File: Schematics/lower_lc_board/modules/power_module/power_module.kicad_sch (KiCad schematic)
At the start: 33 parts, among them J1 Stack Male Edge Connector, U1 TVS3300DRV, U10 ID_LM66100DCKR, U2 AMS1117, U3 ID_LM66100DCKR, U4 ID_LM66100DCKR

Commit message: more local pours and 0402 adjustments
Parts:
- C51, C52: footprint Capacitor_SMD:C_0402_1005Metric -> Capacitor_SMD:C_0603_1608Metric
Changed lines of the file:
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@@
 			)
 		)
-		(property "Footprint" "Capacitor_SMD:C_0402_1005Metric"
+		(property "Footprint" "Capacitor_SMD:C_0603_1608Metric"
 			(at 208.28 61.2648 0)
 			(effects
@@
 			)
 		)
-		(property "Footprint" "Capacitor_SMD:C_0402_1005Metric"
+		(property "Footprint" "Capacitor_SMD:C_0603_1608Metric"
 			(at 208.28 49.8348 0)
 			(effects

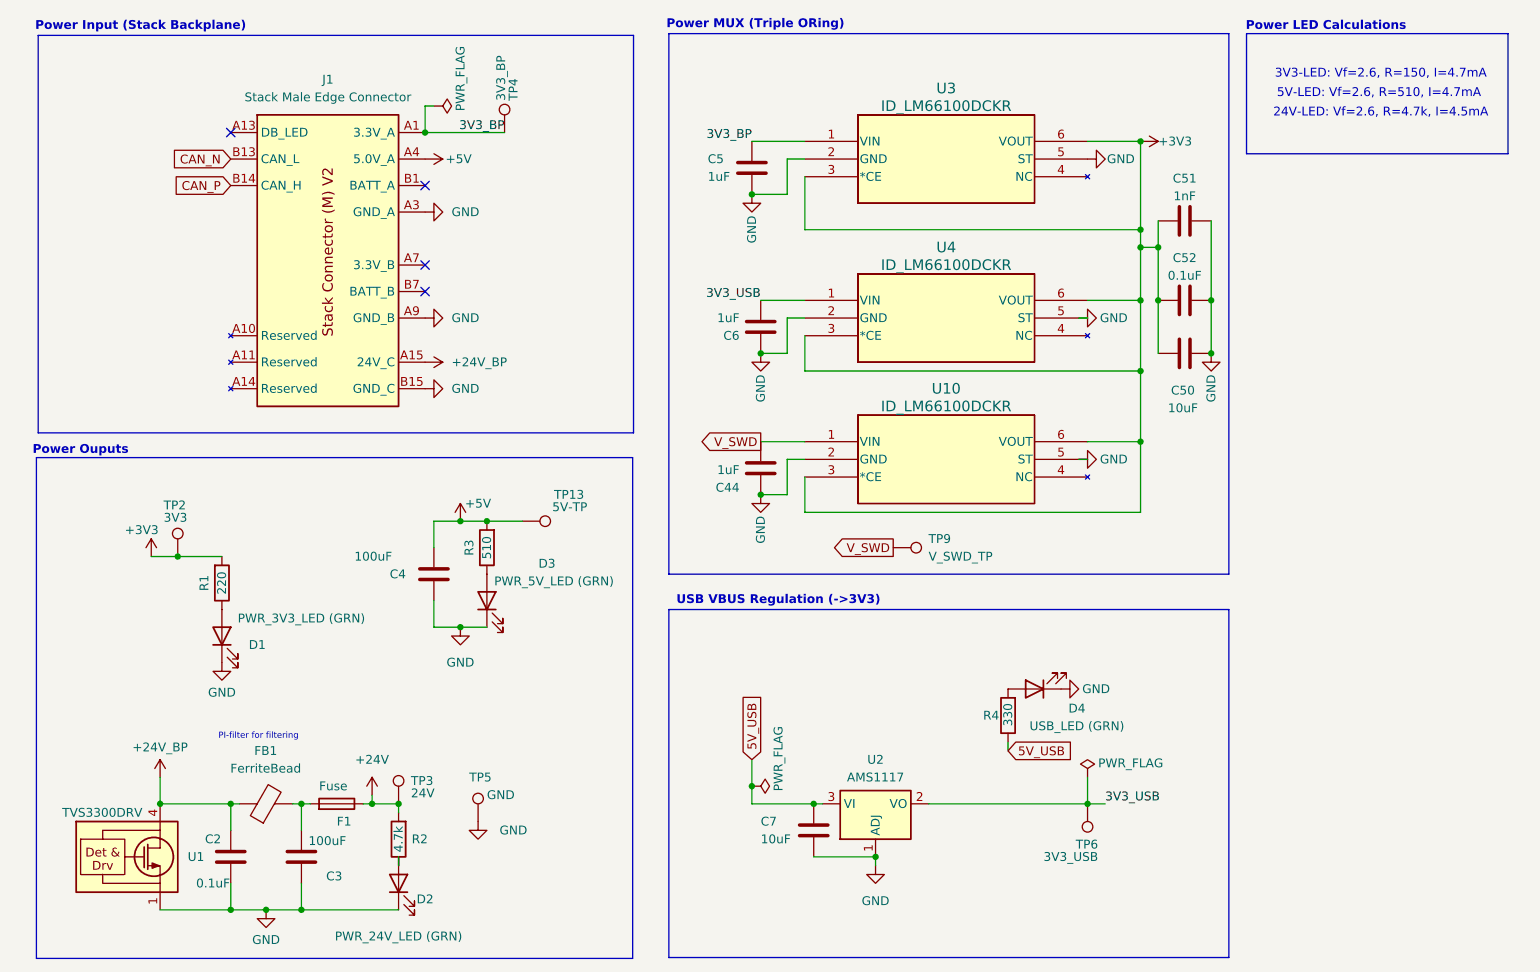
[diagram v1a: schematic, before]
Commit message: review of schematics and pcb
- verified all STM pins
- reviewed all circuits
- reviewed trace clearences, made sure routes are connected, etc.
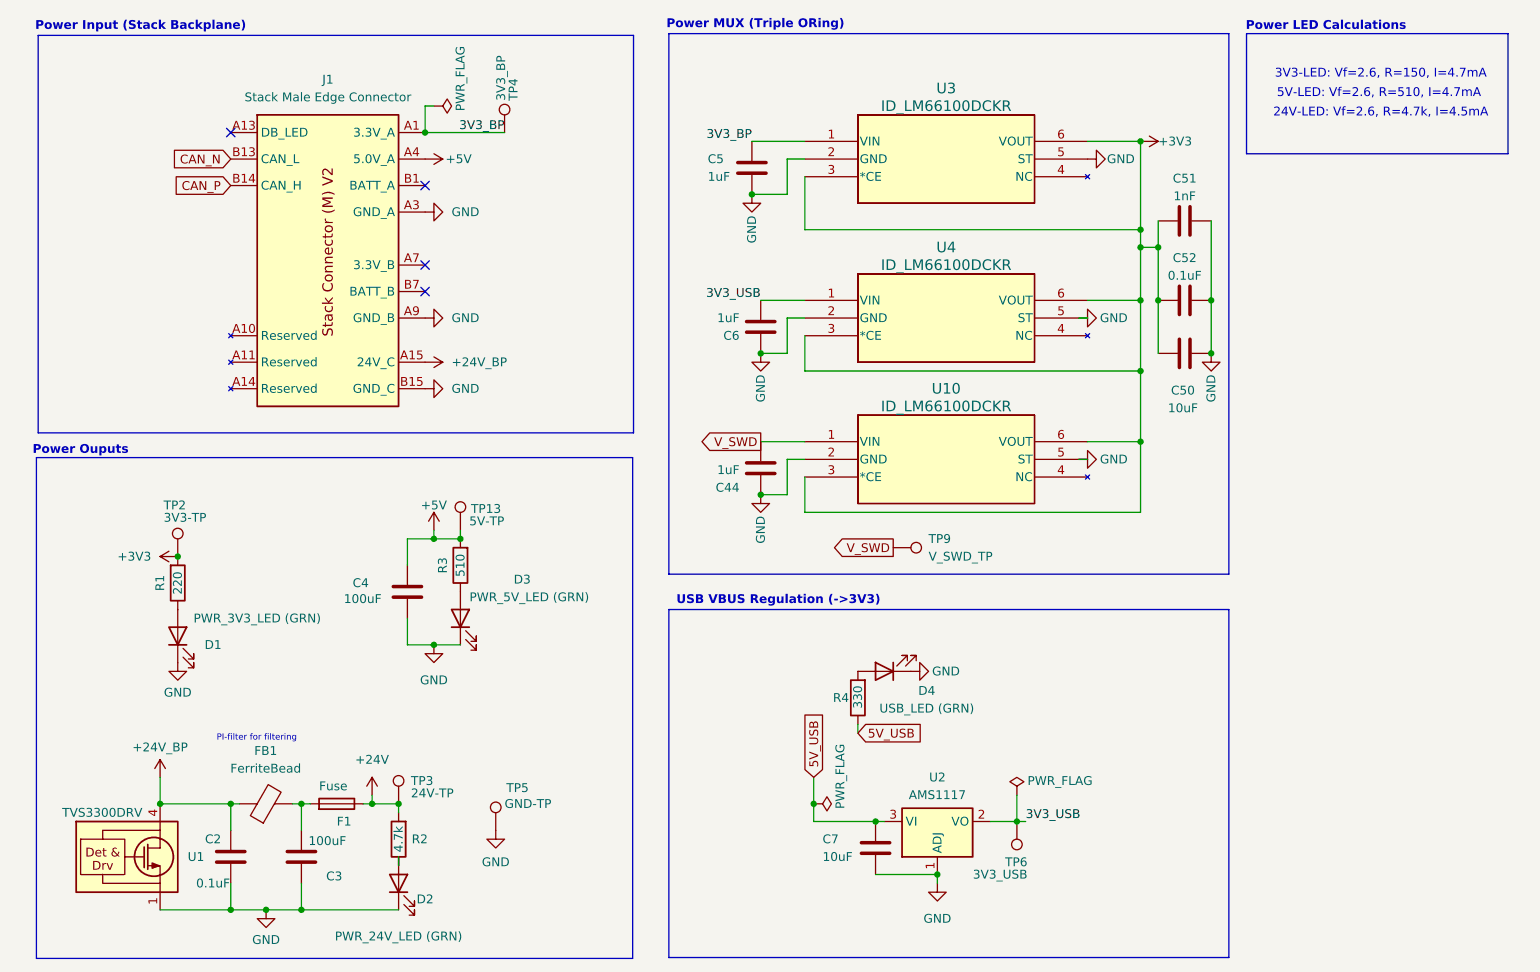
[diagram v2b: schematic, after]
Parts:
- C51: JLCPCB C1523 -> C1588
- C52: JLCPCB C1525 -> C14663
- R2: JLCPCB (none) -> C17936
- TP2: value 3V3 -> 3V3-TP
- TP3: value 24V -> 24V-TP
- TP5: value GND -> GND-TP
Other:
- moved on the sheet: C4, C7, D1, D3, D4, R1, R3, R4, TP13, TP5, TP6, U2

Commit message: silkscreen
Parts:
- removed TP3: 24V-TP, TestPoint:TestPoint_Pad_D1.0mm, symbol Connector:TestPoint
- added TP1: 24V-TP, TestPoint:TestPoint_Pad_D1.0mm, symbol Connector:TestPoint
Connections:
- net +24V: now also TP1.1
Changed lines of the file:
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@@
 	)
 	(junction
-		(at 91.44 134.62)
-		(diameter 0)
-		(color 0 0 0 0)
-	)
-	(junction
 		(at 208.28 69.85)
 		(diameter 0)
@@
 	)
 	(junction
+		(at 91.44 134.62)
+		(diameter 0)
+		(color 0 0 0 0)
+	)
+	(junction
 		(at 67.31 149.86)
 		(diameter 0)
@@
 	)
 	(symbol
-		(lib_id "Connector:TestPoint")
-		(at 91.44 134.62 0)
-		(unit 1)
-		(exclude_from_sim no)
-		(in_bom yes)
-		(on_board yes)
-		(dnp no)
-		(property "Reference" "TP3"
-			(at 93.218 131.318 0)
-			(effects
-				(font
-					(size 1.27 1.27)
-				)
-				(justify left)
-			)
-		)
-		(property "Value" "24V-TP"
-			(at 93.218 133.096 0)
-			(effects
-				(font
-					(size 1.27 1.27)
-				)
-				(justify left)
-			)
-		)
-		(property "Footprint" "TestPoint:TestPoint_Pad_D1.0mm"
-			(at 96.52 134.62 0)
-			(effects
-				(font
-					(size 1.27 1.27)
-				)
-				(hide yes)
-			)
-		)
-		(property "Datasheet" "~"
-			(at 96.52 134.62 0)
-			(effects
-				(font
-					(size 1.27 1.27)
-				)
-				(hide yes)
-			)
-		)
-		(property "Description" "test point"
-			(at 91.44 134.62 0)
-			(effects
-				(font
-					(size 1.27 1.27)
-				)
-				(hide yes)
-			)
-		)
-		(pin "1"
-		)
-		(instances
-			(project "lower_lc_board"
-				(path "/d63798c4-e363-437e-9012-e4aff32e6642/ea1dc739-d1f4-46a0-a090-2a1bf39da427"
-					(reference "TP3")
-					(unit 1)
-				)
-			)
-		)
-	)
-	(symbol
 		(lib_id "power:PWR_FLAG")
 		(at 96.52 34.29 270)
@@
 					(unit 1)
 				)
+			)
+		)
+	)
+	(symbol
+		(lib_id "Connector:TestPoint")
+		(at 91.44 134.62 0)
+		(unit 1)
+		(exclude_from_sim no)
+		(in_bom yes)
+		(on_board yes)
+		(dnp no)
+		(property "Reference" "TP1"
+			(at 93.218 131.318 0)
+			(effects
+				(font
+					(size 1.27 1.27)
+				)
+				(justify left)
+			)
+		)
+		(property "Value" "24V-TP"
+			(at 93.218 133.096 0)
+			(effects
+				(font
+					(size 1.27 1.27)
+				)
+				(justify left)
+			)
+		)
+		(property "Footprint" "TestPoint:TestPoint_Pad_D1.0mm"
+			(at 96.52 134.62 0)
+			(effects
+				(font
+					(size 1.27 1.27)
+				)
+				(hide yes)
+			)
+		)
+		(property "Datasheet" "~"
+			(at 96.52 134.62 0)
+			(effects
+				(font
+					(size 1.27 1.27)
+				)
+				(hide yes)
+			)
+		)
+		(property "Description" "test point"
+			(at 91.44 134.62 0)
+			(effects
+				(font
+					(size 1.27 1.27)
+				)
+				(hide yes)
+			)
+		)
+		(pin "1"
+		)
+		(instances
+			(project "lower_lc_board"
+				(path "/d63798c4-e363-437e-9012-e4aff32e6642/ea1dc739-d1f4-46a0-a090-2a1bf39da427"
+					(reference "TP1")
+					(unit 1)
+				)

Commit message: remove surge protector
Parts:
- removed U1: TVS3300DRV, Package_SON:WSON-6-1EP_2x2mm_P0.65mm_EP1x1.6mm, symbol Power_Protection:TVS3300DRV
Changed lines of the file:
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@@
 	)
 	(junction
-		(at 67.31 149.86)
-		(diameter 0)
-		(color 0 0 0 0)
-	)
-	(junction
 		(at 198.12 82.55)
 		(diameter 0)
@@
 	)
 	(junction
-		(at 57.15 134.62)
-		(diameter 0)
-		(color 0 0 0 0)
-	)
-	(junction
 		(at 59.69 99.06)
 		(diameter 0)
@@
 	(wire
 		(pts
-			(xy 57.15 149.86) (xy 67.31 149.86)
-		)
-		(stroke
-			(width 0)
-			(type default)
-		)
-	)
-	(wire
-		(pts
 			(xy 92.71 96.52) (xy 96.52 96.52)
 		)
@@
 	(wire
 		(pts
-			(xy 57.15 134.62) (xy 57.15 130.81)
-		)
-		(stroke
-			(width 0)
-			(type default)
-		)
-	)
-	(wire
-		(pts
 			(xy 198.12 72.39) (xy 198.12 82.55)
 		)
@@
 	(wire
 		(pts
-			(xy 57.15 134.62) (xy 67.31 134.62)
-		)
-		(stroke
-			(width 0)
-			(type default)
-		)
-	)
-	(wire
-		(pts
 			(xy 95.25 34.29) (xy 96.52 34.29)
 		)
@@
 	)
 	(symbol
-		(lib_id "Power_Protection:TVS3300DRV")
-		(at 57.15 142.24 0)
-		(unit 1)
-		(exclude_from_sim no)
-		(in_bom yes)
-		(on_board yes)
-		(dnp no)
-		(property "Reference" "U1"
-			(at 63.5 142.24 0)
-			(effects
-				(font
-					(size 1.27 1.27)
-				)
-				(justify right)
-			)
-		)
-		(property "Value" "TVS3300DRV"
-			(at 54.61 135.89 0)
-			(effects
-				(font
-					(size 1.27 1.27)
-				)
-				(justify right)
-			)
-		)
-		(property "Footprint" "Package_SON:WSON-6-1EP_2x2mm_P0.65mm_EP1x1.6mm"
-			(at 62.23 151.13 0)
-			(effects
-				(font
-					(size 1.27 1.27)
-				)
-				(hide yes)
-			)
-		)
-		(property "Datasheet" "${KIPRJMOD}/../../Documentation/surgeprot_tvs3300_DS.pdf"
-			(at 54.61 142.24 0)
-			(effects
-				(font
-					(size 1.27 1.27)
-				)
-				(hide yes)
-			)
-		)
-		(property "Description" "Flat-Clamp Surge Protection Device. 33Vrwm, WSON-6"
-			(at 57.15 142.24 0)
-			(effects
-				(font
-					(size 1.27 1.27)
-				)
-				(hide yes)
-			)
-		)
-		(property "LCSC" "C2863624"
-			(at 57.15 142.24 0)
-			(effects
-				(font
-					(size 1.27 1.27)
-				)
-				(hide yes)
-			)
-		)
-		(pin "7"
-		)
-		(pin "6"
-		)
-		(pin "4"
-		)
-		(pin "5"
-		)
-		(pin "1"
-		)
-		(pin "3"
-		)
-		(pin "2"
-		)
-		(instances
-			(project "lower_lc_board"
-				(path "/d63798c4-e363-437e-9012-e4aff32e6642/ea1dc739-d1f4-46a0-a090-2a1bf39da427"
-					(reference "U1")
-					(unit 1)
-				)
-			)
-		)
-	)
-	(symbol
 		(lib_id "Connector:TestPoint")
 		(at 180.34 137.16 180)
@@
 	(symbol
 		(lib_id "power:+24V")
-		(at 57.15 130.81 0)
+		(at 67.31 134.62 90)
 		(unit 1)
 		(exclude_from_sim no)
@@
 		(dnp no)
 		(property "Reference" "#PWR02"
-			(at 57.15 134.62 0)
+			(at 71.12 134.62 0)
 			(effects
 				(font
@@
 		)
 		(property "Value" "+24V_BP"
-			(at 57.15 126.492 0)
+			(at 59.182 134.62 90)
 			(effects
 				(font
@@
 		)
 		(property "Footprint" ""
-			(at 57.15 130.81 0)
+			(at 67.31 134.62 0)
 			(effects
 				(font
@@
 		)
 		(property "Datasheet" ""
-			(at 57.15 130.81 0)
+			(at 67.31 134.62 0)
 			(effects
 				(font
@@
 		)
 		(property "Description" "Power symbol creates a global label with name \"+24V\""
-			(at 57.15 130.81 0)
+			(at 67.31 134.62 0)
 			(effects
 				(font

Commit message: put TH on backside, add edge-vias
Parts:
- added TP3: GND-TP-H, TestPoint:TestPoint_THTPad_D1.0mm_Drill0.5mm, symbol Connector:TestPoint
- TP5: value GND-TP -> GND-TP-P; footprint TestPoint:TestPoint_Pad_D1.0mm -> TestPoint:TestPoint_Pad_1.5x1.5mm
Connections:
- net GND: now also TP3.1
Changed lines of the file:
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@@
 			)
 		)
-		(property "Value" "GND-TP"
+		(property "Value" "GND-TP-P"
 			(at 106.68 134.62 0)
 			(effects
@@
 			)
 		)
-		(property "Footprint" "TestPoint:TestPoint_Pad_D1.0mm"
+		(property "Footprint" "TestPoint:TestPoint_Pad_1.5x1.5mm"
 			(at 110.49 138.43 0)
 			(effects
@@
 	)
 	(symbol
+		(lib_id "Connector:TestPoint")
+		(at 111.76 143.51 0)
+		(unit 1)
+		(exclude_from_sim no)
+		(in_bom yes)
+		(on_board yes)
+		(dnp no)
+		(property "Reference" "TP3"
+			(at 113.284 137.414 0)
+			(effects
+				(font
+					(size 1.27 1.27)
+				)
+				(justify left)
+			)
+		)
+		(property "Value" "GND-TP-H"
+			(at 113.03 139.7 0)
+			(effects
+				(font
+					(size 1.27 1.27)
+				)
+				(justify left)
+			)
+		)
+		(property "Footprint" "TestPoint:TestPoint_THTPad_D1.0mm_Drill0.5mm"
+			(at 116.84 143.51 0)
+			(effects
+				(font
+					(size 1.27 1.27)
+				)
+				(hide yes)
+			)
+		)
+		(property "Datasheet" "~"
+			(at 116.84 143.51 0)
+			(effects
+				(font
+					(size 1.27 1.27)
+				)
+				(hide yes)
+			)
+		)
+		(property "Description" "test point"
+			(at 111.76 143.51 0)
+			(effects
+				(font
+					(size 1.27 1.27)
+				)
+				(hide yes)
+			)
+		)
+		(pin "1"
+		)
+		(instances
+			(project "lower_lc_board"
+				(path "/d63798c4-e363-437e-9012-e4aff32e6642/ea1dc739-d1f4-46a0-a090-2a1bf39da427"
+					(reference "TP3")
+					(unit 1)
+				)
+			)
+		)
+	)
+	(symbol
 		(lib_id "QRET_Buck_PSU:LM66100DCKR")
 		(at 170.18 64.77 0)
@@
 					(unit 1)
 				)
+			)
+		)
+	)
+	(symbol
+		(lib_id "power:GND")
+		(at 111.76 143.51 0)
+		(unit 1)
+		(exclude_from_sim no)
+		(in_bom yes)
+		(on_board yes)
+		(dnp no)
+		(property "Reference" "#PWR0109"
+			(at 111.76 149.86 0)
+			(effects
+				(font
+					(size 1.27 1.27)
+				)
+				(hide yes)
+			)
+		)
+		(property "Value" "GND"
+			(at 111.76 148.082 0)
+			(effects
+				(font
+					(size 1.27 1.27)
+				)
+			)
+		)
+		(property "Footprint" ""
+			(at 111.76 143.51 0)
+			(effects
+				(font
+					(size 1.27 1.27)
+				)
+				(hide yes)
+			)
+		)
+		(property "Datasheet" ""
+			(at 111.76 143.51 0)
+			(effects
+				(font
+					(size 1.27 1.27)
+				)
+				(hide yes)
+			)
+		)
+		(property "Description" "Power symbol creates a global label with name \"GND\" , ground"
+			(at 111.76 143.51 0)
+			(effects
+				(font
+					(size 1.27 1.27)
+				)
+				(hide yes)
+			)
+		)
+		(pin "1"
+		)
+		(instances
+			(project "lower_lc_board"
+				(path "/d63798c4-e363-437e-9012-e4aff32e6642/ea1dc739-d1f4-46a0-a090-2a1bf39da427"
+					(reference "#PWR0109")
+					(unit 1)
+				)

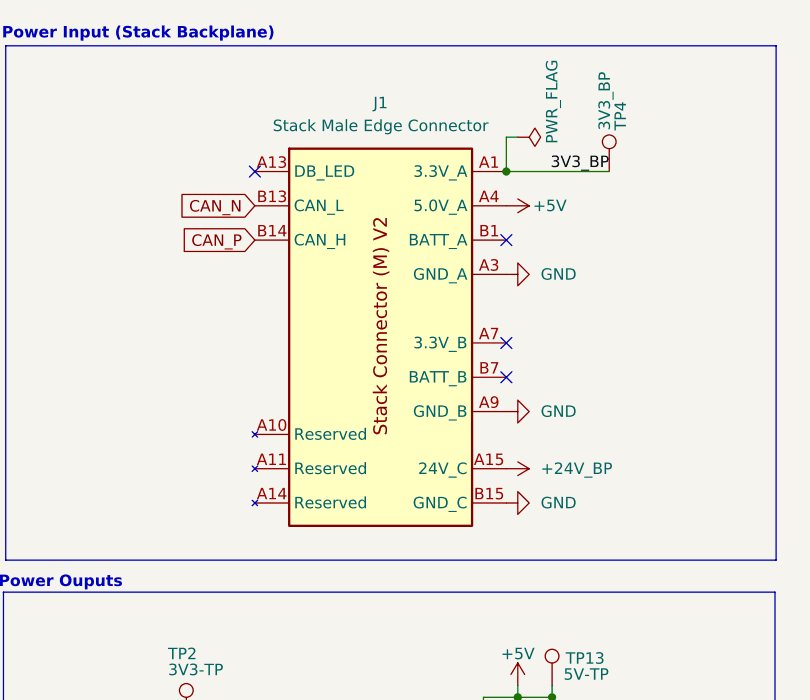
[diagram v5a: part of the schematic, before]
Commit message: new backplane connector
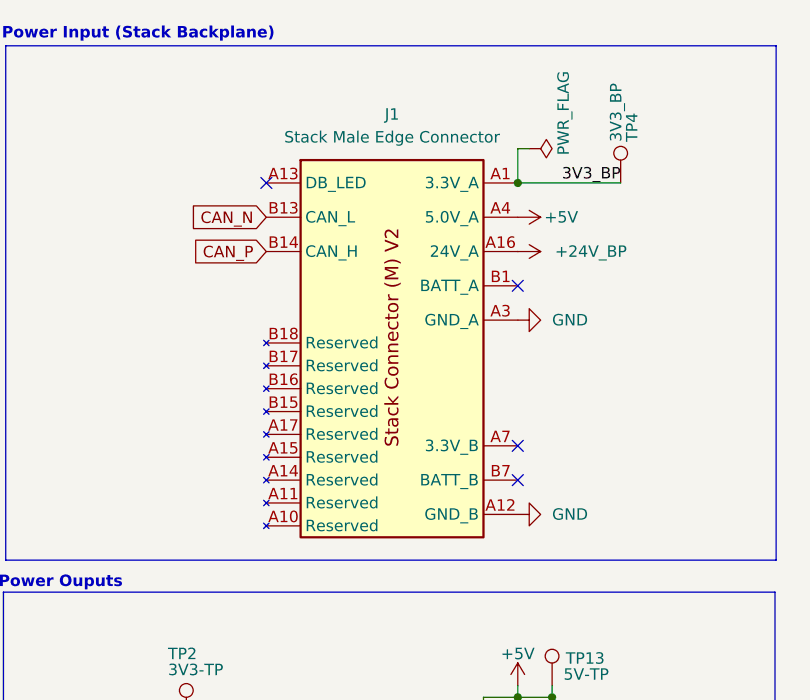
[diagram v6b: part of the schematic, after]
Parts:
- removed J1: Stack Male Edge Connector, Connector_PCBEdge:BUS_PCIexpress_x1, symbol EdgeConnector:Stack Male Edge Connector
- added J1: Stack Male Edge Connector, Connector_PCBEdge:BUS_PCIexpress_x1, symbol EdgeConnectorV2:Stack Male Edge Connector
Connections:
- net +24V_BP: now also J1.A16 (24V_A), J1.A18 (24V_A)
- net +5V: now also J1.A4 (5.0V_A), J1.A5 (5.0V_A)
- net 3V3_BP: now also J1.A1 (3.3V_A), J1.A2 (3.3V_A)
- net CAN_N: now also J1.B13 (CAN_L)
- net CAN_P: now also J1.B14 (CAN_H)
- net GND: now also J1.A12 (GND_B), J1.A3 (GND_A), J1.A6 (GND_A), J1.A9 (GND_B), J1.B10 (GND_B), J1.B11 (GND_B), J1.B12 (GND_B), J1.B4 (GND_A), J1.B5 (GND_A), J1.B6 (GND_A)
- new net: J1.A7 (3.3V_B), J1.A8 (3.3V_B)
- new net: J1.B1 (BATT_A), J1.B2 (BATT_A), J1.B3 (BATT_A)
- new net: J1.B7 (BATT_B), J1.B8 (BATT_B), J1.B9 (BATT_B)

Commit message: increase width on power rails from USB and SWD, start tuning diff pairs
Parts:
- C4: Digikey 732-8419-1-ND -> 732-8511-1-ND
- D1, D2, D3, D4: Digikey (none) -> 150080VS75000
- R1: JLCPCB (none) -> C22962
- R2: Digikey 311-4.70KFRCT-ND -> (none)
- R3: JLCPCB (none) -> C23186
- R4: JLCPCB (none) -> C23138
- U10, U3, U4: JLCPCB (none) -> C2869734
- U2: Digikey (none) -> 5399-AMS1117-3.3SOT-223TR-ND
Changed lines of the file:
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@@
 			)
 		)
+		(property "JLCPCB" "C2869734"
+			(at 170.18 41.91 0)
+			(effects
+				(font
+					(size 1.27 1.27)
+				)
+				(hide yes)
+			)
+		)
 		(pin "1"
 		)
@@
 			)
 		)
+		(property "JLCPCB" "C23138"
+			(at 157.48 119.38 0)
+			(effects
+				(font
+					(size 1.27 1.27)
+				)
+				(hide yes)
+			)
+		)
 		(pin "2"
 		)
@@
 			)
 		)
+		(property "Digikey" "150080VS75000"
+			(at 100.33 107.95 0)
+			(effects
+				(font
+					(size 1.27 1.27)
+				)
+				(hide yes)
+			)
+		)
 		(pin "2"
 		)
@@
 			)
 		)
-		(property "JLCPCB" ""
+		(property "JLCPCB" "C22962"
 			(at 59.69 102.87 0)
 			(effects
@@
 			)
 		)
+		(property "JLCPCB" "C2869734"
+			(at 170.18 85.09 0)
+			(effects
+				(font
+					(size 1.27 1.27)
+				)
+				(hide yes)
+			)
+		)
 		(pin "1"
 		)
@@
 			)
 		)
+		(property "JLCPCB" "C23186"
+			(at 100.33 100.33 0)
+			(effects
+				(font
+					(size 1.27 1.27)
+				)
+				(hide yes)
+			)
+		)
 		(pin "2"
 		)
@@
 			)
 		)
+		(property "Digikey" "150080VS75000"
+			(at 161.29 115.57 0)
+			(effects
+				(font
+					(size 1.27 1.27)
+				)
+				(hide yes)
+			)
+		)
 		(pin "2"
 		)
@@
 			)
 		)
+		(property "JLCPCB" "C2869734"
+			(at 170.18 64.77 0)
+			(effects
+				(font
+					(size 1.27 1.27)
+				)
+				(hide yes)
+			)
+		)
 		(pin "1"
 		)
@@
 			)
 		)
-		(property "Digikey" "732-8419-1-ND"
+		(property "Digikey" "732-8511-1-ND"
 			(at 92.71 104.14 0)
 			(effects
@@
 			)
 		)
-		(property "Digikey" "311-4.70KFRCT-ND"
+		(property "Digikey" ""
 			(at 91.44 139.7 90)
 			(effects
@@
 			)
 		)
+		(property "Digikey" "150080VS75000"
+			(at 59.69 110.49 0)
+			(effects
+				(font
+					(size 1.27 1.27)
+				)
+				(hide yes)
+			)
+		)
 		(pin "2"
 		)
@@
 			)
 		)
+		(property "Digikey" "5399-AMS1117-3.3SOT-223TR-ND"
+			(at 168.91 137.16 0)
+			(effects
+				(font
+					(size 1.27 1.27)
+				)
+				(hide yes)
+			)
+		)
 		(pin "3"
 		)
@@
 			(effects
 				(font
+					(size 1.27 1.27)
+				)
+				(hide yes)
+			)
+		)
+		(property "Digikey" "150080VS75000"
+			(at 91.44 146.05 0)
+			(effects
+				(font

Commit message: start lower refactor
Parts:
- removed J1: Stack Male Edge Connector, Connector_PCBEdge:BUS_PCIexpress_x1, symbol EdgeConnectorV2:Stack Male Edge Connector
- added C1: 10uF, Capacitor_SMD:CP_Elec_4x5.4, symbol Device:C_Polarized
- added J1: Conn_01x06, CONN_SD-4:CONN_SD-43045-001_06_MOL, symbol Connector_Generic:Conn_01x06
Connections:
- net +24V_BP: now also J1.4 (Pin_4)
- net +3V3: now also C1.1
- net +5V: now also J1.5 (Pin_5)
- net 3V3_BP: now also J1.6 (Pin_6)
- net CAN_N: now also J1.2 (Pin_2)
- net CAN_P: now also J1.3 (Pin_3)
- net GND: now also C1.2, J1.1 (Pin_1)
- no-connect marks 4 -> 0
